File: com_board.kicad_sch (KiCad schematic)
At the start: 28 parts, among them J1 USB_C_Receptacle_USB2.0_16P, J2 Conn_ST_STDC14, U1 nRF52820-QDxx, U2 USBLC6-2SC6, Y1 32.768kHz Cl=9pF, Y2 32MHz Cl=8pF

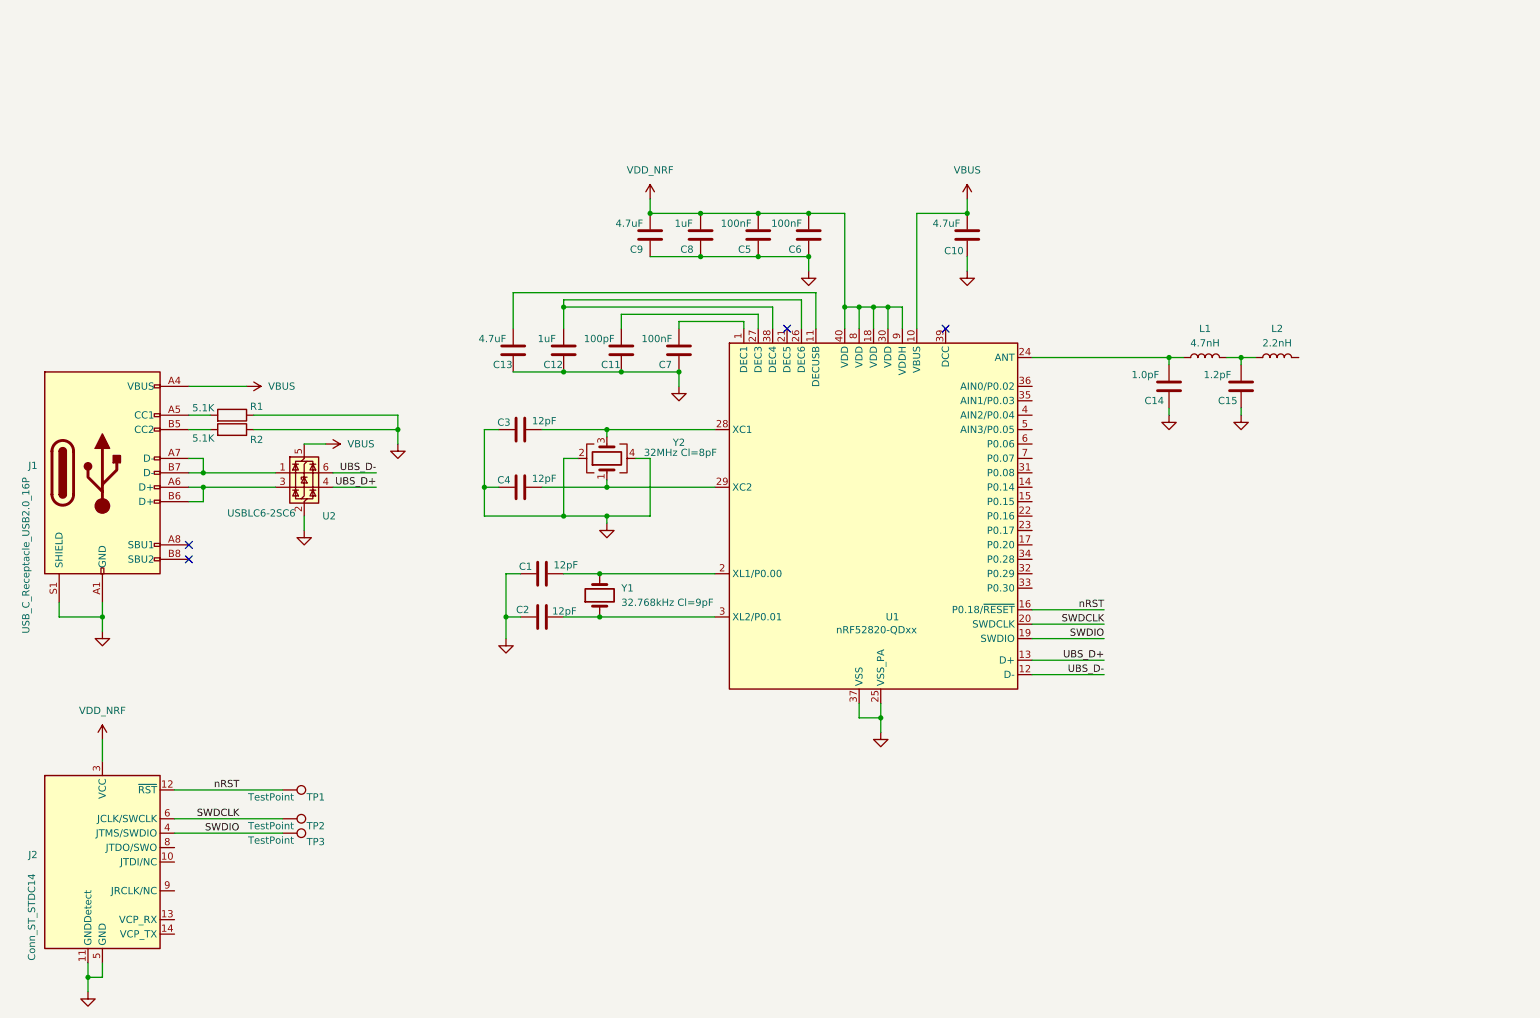
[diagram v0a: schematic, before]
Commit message: Added uwb module
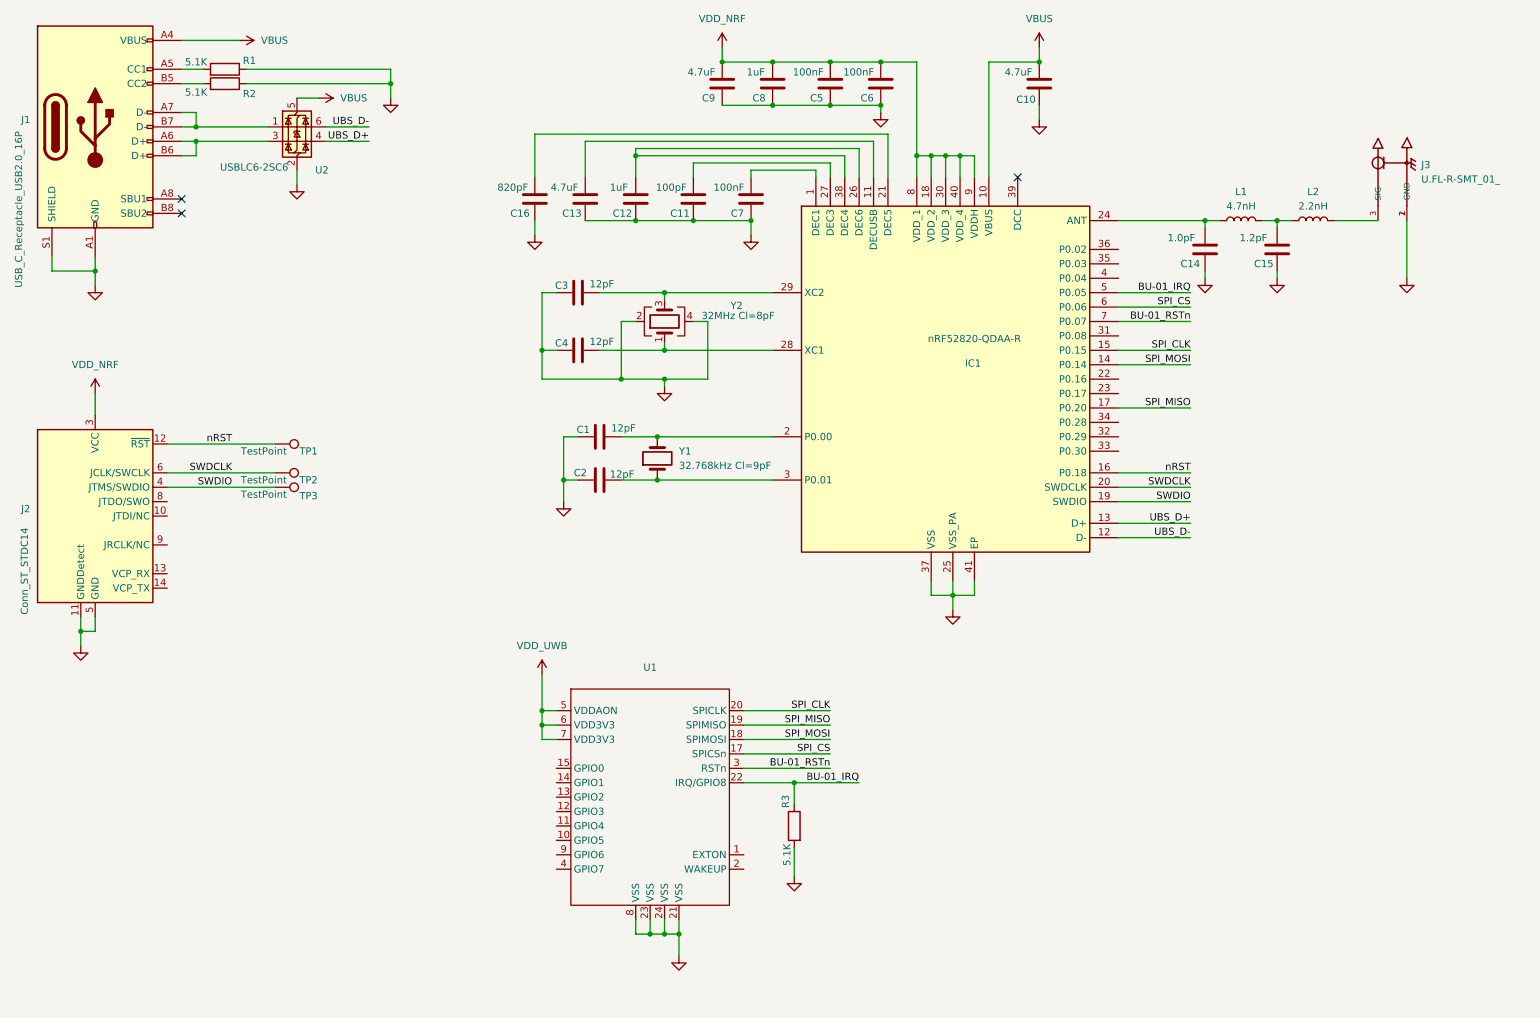
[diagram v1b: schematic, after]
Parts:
- removed U1: nRF52820-QDxx, Package_DFN_QFN:QFN-40-1EP_5x5mm_P0.4mm_EP3.6x3.6mm, symbol MCU_Nordic:nRF52820-QDxx
- added C16: 820pF, Capacitor_SMD:C_0201_0603Metric, symbol Device:C
- added IC1: nRF52820-QDAA-R, QFN40P500X500X90-41N-D, symbol nRF52820-QDAA-R:nRF52820-QDAA-R
- added J3: U.FL-R-SMT_01_, U:HRS_U.FL-R-SMT_01_, symbol U.FL-R-SMT_01_:U.FL-R-SMT_01_
- added R3: 5.1K, Resistor_SMD:R_0402_1005Metric_Pad0.72x0.64mm_HandSolder, symbol Device:R
- added U1: ~, symbol bu-01:_1
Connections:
- net GND: now also C16.2, IC1.25 (VSS_PA), IC1.37 (VSS), IC1.41 (EP), J3.1 (GND), J3.2 (GND), R3.2, U1.21 (VSS), U1.23 (VSS), U1.24 (VSS), U1.8 (VSS)
- net SWDCLK: now also IC1.20 (SWDCLK)
- net SWDIO: now also IC1.19 (SWDIO)
- net UBS_D+: now also IC1.13 (D+)
- net UBS_D-: now also IC1.12 (D-)
- net VBUS: now also IC1.10 (VBUS)
- net VDD_NRF: now also IC1.18 (VDD_2), IC1.30 (VDD_3), IC1.40 (VDD_4), IC1.8 (VDD_1), IC1.9 (VDDH)
- net nRST: now also IC1.16 (P0.18)
- net at C1.1, Y1.2: now also IC1.2 (P0.00)
- net at L2.2: now also J3.3 (SIG)
- net at C4.1, Y2.1: now also IC1.28 (XC1)
- net at C3.1, Y2.3: now also IC1.29 (XC2)
- net at C7.1: now also IC1.1 (DEC1)
- net at C13.1: now also IC1.11 (DECUSB)
- net at C14.1, L1.1: now also IC1.24 (ANT)
- net at C12.1: now also IC1.26 (DEC6), IC1.38 (DEC4)
- net at C11.1: now also IC1.27 (DEC3)
- net at C2.1, Y1.1: now also IC1.3 (P0.01)
- new net: C16.1, IC1.21 (DEC5)
- new net BU-01_IRQ: IC1.5 (P0.05), R3.1, U1.22 (IRQ/GPIO8)
- new net BU-01_RSTn: IC1.7 (P0.07), U1.3 (RSTn)
- new net SPI_CLK: IC1.15 (P0.15), U1.20 (SPICLK)
- new net SPI_CS: IC1.6 (P0.06), U1.17 (SPICSn)
- new net SPI_MISO: IC1.17 (P0.20), U1.19 (SPIMISO)
- new net SPI_MOSI: IC1.14 (P0.14), U1.18 (SPIMOSI)
- new net VDD_UWB: U1.5 (VDDAON), U1.6 (VDD3V3), U1.7 (VDD3V3)
- no-connect marks 4 -> 3
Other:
- moved on the sheet: C1, C10, C11, C12, C13, C14, C15, C2, C3, C4, C5, C6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

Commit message: Finished schematic
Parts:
- added C17, C18: 1uF, Capacitor_SMD:C_0402_1005Metric_Pad0.74x0.62mm_HandSolder, symbol Device:C
- added H1, H2, H3, H4: MountingHole, MountingHole:MountingHole_2.2mm_M2, symbol Mechanical:MountingHole
- added JP1: SolderJumper_3_Open, Jumper:SolderJumper-3_P1.3mm_Open_Pad1.0x1.5mm_NumberLabels, symbol Jumper:SolderJumper_3_Open
- added POW_5V1: FFC-FPC:TE_84952_4, Connector_FFC-FPC:TE_84952-4_1x04-1MP_P1.0mm_Horizontal, symbol Connector_Generic_MountingPin:Conn_01x04_MountingPin
- added TP10, TP11, TP12, TP13, TP14, TP15, TP4, TP5, TP6, TP7, TP8, TP9: TestPoint, TestPoint:TestPoint_Pad_D1.0mm, symbol Connector:TestPoint
- added U5: AP2112K-3.3, Package_TO_SOT_SMD:SOT-23-5, symbol Regulator_Linear:AP2112K-3.3
- IC1: footprint QFN40P500X500X90-41N-D -> NRF52qdaa:QFN40P500X500X90-41N-D
- U1: value ~ -> BU-01; footprint (none) -> bu-01:BU-01
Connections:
- net VDD_UWB is gone; now on net 3.3V_VDD: U1.5 (VDDAON), U1.6 (VDD3V3), U1.7 (VDD3V3)
- net BU-01_IRQ: now also TP13.1
- net BU-01_RSTn: now also TP12.1
- net GND: now also C17.2, C18.2, POW_5V1.4 (Pin_4), POW_5V1.MP (MountPin), U5.2 (GND)
- net SPI_CLK: now also TP10.1
- net SPI_CS: now also TP11.1
- net SPI_MISO: now also TP8.1
- net SPI_MOSI: now also TP9.1
- net UBS_D+: now also TP14.1
- net UBS_D-: now also TP15.1
- net VBUS: now also JP1.3 (B)
- net UART_RX: now reaches IC1.36 (P0.02)
- net UART_RX: now also POW_5V1.2 (Pin_2), TP6.1
- net UART_TX: now reaches IC1.4 (P0.04)
- net UART_TX: now also POW_5V1.3 (Pin_3), TP7.1
- net VDD_NRF renamed 3.3V_VDD
- net 3.3V_VDD: now also C17.1, TP4.1, U5.5 (VOUT)
- new net: C18.1, JP1.2 (C), TP5.1, U5.1 (VIN)
- new net 5V_VDD: JP1.1 (A), POW_5V1.1 (Pin_1)
- new net POWER_EN: U5.3 (EN)
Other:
- note added: "Connectors"
- note added: "Debug connectors"
- note added: "Mounting"
- note added: "NRF52820"
- note added: "Regulator"
- note added: "UWB"
- moved on the sheet: C1, C10, C11, C12, C13, C14, C15, C16, C2, C3, C4, C5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

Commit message: Fixed libs
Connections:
- net GND: now also U1.16 (VSS)
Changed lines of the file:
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@@
 	)
 	(junction
+		(at 133.35 189.23)
+		(diameter 0)
+		(color 0 0 0 0)
+	)
+	(junction
 		(at 143.51 34.29)
 		(diameter 0)
@@
 	(wire
 		(pts
+			(xy 130.81 186.69) (xy 130.81 189.23)
+		)
+		(stroke
+			(width 0)
+			(type default)
+		)
+	)
+	(wire
+		(pts
 			(xy 63.5 38.1) (xy 50.8 38.1)
 		)
@@
 	(wire
 		(pts
+			(xy 130.81 189.23) (xy 133.35 189.23)
+		)
+		(stroke
+			(width 0)
+			(type default)
+		)
+	)
+	(wire
+		(pts
 			(xy 138.43 189.23) (xy 135.89 189.23)
 		)
@@
 		(pin "1"
 		)
+		(pin "16"
+		)
 		(instances

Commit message: Almost done
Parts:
- J3: footprint U:HRS_U.FL-R-SMT_01_ -> UFL:HRS_U.FL-R-SMT_01_
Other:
- note added: "PLACE POWER ENABLE PIN FRON REGULATOR TO CONNECTOR!!!!!!!"
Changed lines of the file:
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@@
 		)
 	)
+	(text "PLACE POWER ENABLE PIN FRON REGULATOR TO CONNECTOR!!!!!!!"
+		(exclude_from_sim no)
+		(at 170.434 130.81 0)
+		(effects
+			(font
+				(size 7.62 7.62)
+				(thickness 1.524)
+				(bold yes)
+				(color 255 0 11 1)
+			)
+		)
+	)
 	(text "NRF52820\n"
 		(exclude_from_sim no)
@@
 			)
 		)
-		(property "Footprint" "U:HRS_U.FL-R-SMT_01_"
+		(property "Footprint" "UFL:HRS_U.FL-R-SMT_01_"
 			(at 252.73 52.07 0)
 			(effects

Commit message: first iteration
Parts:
- removed POW_5V1: FFC-FPC:TE_84952_4, Connector_FFC-FPC:TE_84952-4_1x04-1MP_P1.0mm_Horizontal, symbol Connector_Generic_MountingPin:Conn_01x04_MountingPin
- removed TP14, TP15: TestPoint, TestPoint:TestPoint_Pad_D1.0mm, symbol Connector:TestPoint
- added TP16, TP17: TestPoint, TestPoint:TestPoint_Pad_D1.0mm, symbol Connector:TestPoint
- added UART_conn1: FFC-FPC:TE_84952_6, Connector_FFC-FPC:TE_84952-6_1x06-1MP_P1.0mm_Horizontal, symbol Connector_Generic_MountingPin:Conn_01x06_MountingPin
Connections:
- net 5V_VDD: now also UART_conn1.1 (Pin_1)
- net GND: now also UART_conn1.6 (Pin_6), UART_conn1.MP (MountPin)
- net POWER_EN: now also TP16.1, UART_conn1.2 (Pin_2)
- net UART_RX: now also UART_conn1.4 (Pin_4)
- net UART_TX: now also UART_conn1.5 (Pin_5)
- net INT: now reaches IC1.33 (P0.30)
- net INT: now also TP17.1, UART_conn1.3 (Pin_3)
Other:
- note added: "CHECK THAT 4 PAD AND 2 PAD CRYSTAL TO SEE IF IT MATCHES WITH THE CAPS"
- note removed: "PLACE POWER ENABLE PIN FRON REGULATOR TO CONNECTOR!!!!!!!"
- moved on the sheet: TP6, TP7
